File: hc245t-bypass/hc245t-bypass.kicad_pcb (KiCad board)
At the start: 2 copper layers, 6.6 x 4.5 mm, 16 parts

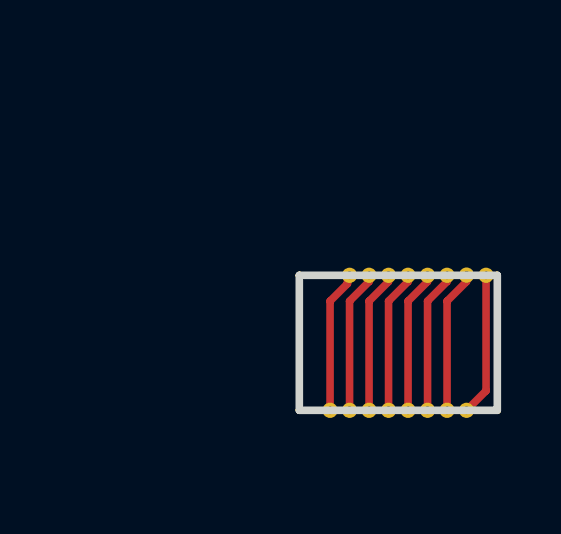
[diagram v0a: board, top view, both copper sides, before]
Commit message: hc245t-bypass: create panel of two to account for oshpark min size
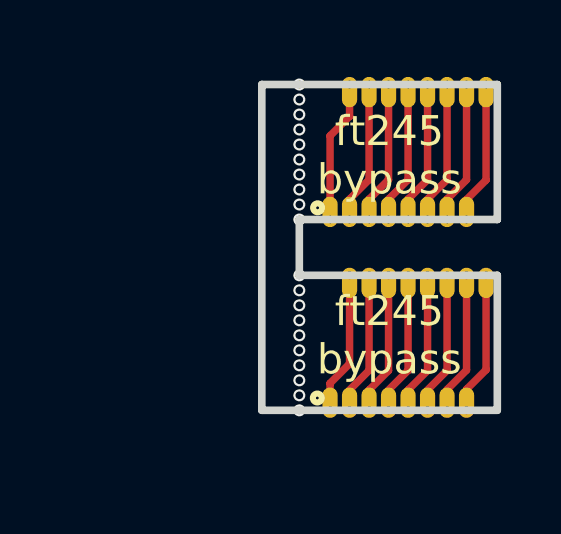
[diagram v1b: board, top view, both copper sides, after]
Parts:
- added TP21: TestPoint, tom-mechanical:Castellation_5.08_2.54, F.Cu at (-2.27, -4.11)
- added TP22: TestPoint, tom-mechanical:Castellation_5.08_2.54, F.Cu at (-1.62, -4.11)
- added TP23: TestPoint, tom-mechanical:Castellation_5.08_2.54, F.Cu at (-0.97, -4.11)
- added TP24: TestPoint, tom-mechanical:Castellation_5.08_2.54, F.Cu at (0.33, -8.61)
- added TP25: TestPoint, tom-mechanical:Castellation_5.08_2.54, F.Cu at (0.33, -4.11)
- added TP26: TestPoint, tom-mechanical:Castellation_5.08_2.54, F.Cu at (0.97, -4.11)
- added TP27: TestPoint, tom-mechanical:Castellation_5.08_2.54, F.Cu at (1.62, -4.11)
- added TP29: TestPoint, tom-mechanical:Castellation_5.08_2.54, F.Cu at (-1.62, -8.61)
- added TP30: TestPoint, tom-mechanical:Castellation_5.08_2.54, F.Cu at (-0.97, -8.61)
- added TP31: TestPoint, tom-mechanical:Castellation_5.08_2.54, F.Cu at (-0.33, -8.61)
- added TP32: TestPoint, tom-mechanical:Castellation_5.08_2.54, F.Cu at (-0.33, -4.11)
- added TP33: TestPoint, tom-mechanical:Castellation_5.08_2.54, F.Cu at (0.97, -8.61)
- added TP34: TestPoint, tom-mechanical:Castellation_5.08_2.54, F.Cu at (1.62, -8.61)
- added TP35: TestPoint, tom-mechanical:Castellation_5.08_2.54, F.Cu at (2.27, -8.61)
- added TP36: TestPoint, tom-mechanical:Castellation_5.08_2.54, F.Cu at (2.92, -8.61)
- added TP9: TestPoint, tom-mechanical:Castellation_5.08_2.54, F.Cu at (2.27, -4.11)
- turned TP2 to 180 degrees
- turned TP3 to 180 degrees
- turned TP4 to 180 degrees
- turned TP5 to 180 degrees
- turned TP6 to 180 degrees
- turned TP7 to 180 degrees
- turned TP8 to 180 degrees
- turned TP9 to 180 degrees
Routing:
- net /a7b7: track 0.00 -> 4.77 mm
- net /a6b6: track 0.00 -> 4.77 mm
- net /a5b5: track 0.00 -> 4.77 mm
- net /a4b4: track 0.00 -> 4.77 mm
- net /a3b3: track 0.00 -> 4.77 mm
- net /a2b2: track 0.00 -> 4.77 mm
- net /a1b1: track 0.00 -> 4.77 mm
- net /a0b0: track 0.00 -> 4.77 mm
- net (no net): vias 0 -> 20
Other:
- board size 6.6 x 4.5 mm -> 7.8 x 10.9 mm
- rule via_min_drill: 0.3 -> 0.254
- board text added: "Jan2020"
- board text added: "ft245 bypass"

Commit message: hc245t-bypass: Feb 2020 version, increase spacing between boards
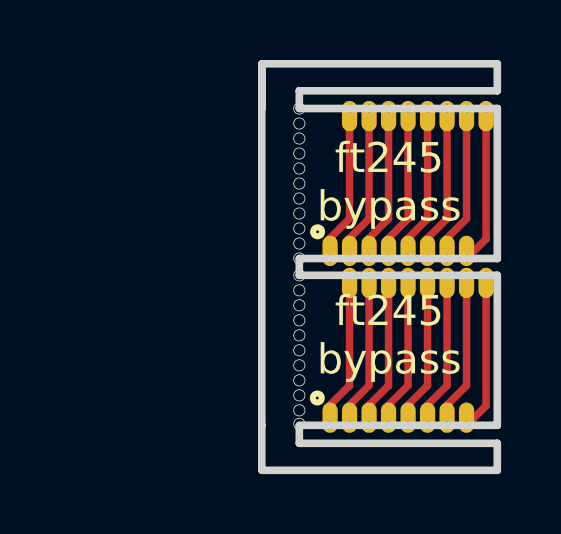
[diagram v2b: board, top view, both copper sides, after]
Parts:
- moved TP21 1.30 mm to (-2.27, -2.81)
- moved TP22 1.30 mm to (-1.62, -2.81)
- moved TP23 1.30 mm to (-0.97, -2.81)
- moved TP25 1.30 mm to (0.33, -2.81)
- moved TP26 1.30 mm to (0.97, -2.81)
- moved TP27 1.30 mm to (1.62, -2.81)
- moved TP32 1.30 mm to (-0.33, -2.81)
- moved TP9 1.30 mm to (2.27, -2.81)
- moved TP24 0.80 mm to (0.33, -7.81)
- moved TP29 0.80 mm to (-1.62, -7.81)
- moved TP30 0.80 mm to (-0.97, -7.81)
- moved TP31 0.80 mm to (-0.33, -7.81)
- moved TP33 0.80 mm to (0.97, -7.81)
- moved TP34 0.80 mm to (1.62, -7.81)
- moved TP35 0.80 mm to (2.27, -7.81)
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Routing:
- net /A2B2: track 4.77 -> 5.28 mm
- net /A0B0: track 4.77 -> 5.28 mm
- net /a7b7: track 4.77 -> 5.27 mm
- net /a6b6: track 4.77 -> 5.27 mm
- net /a5b5: track 4.77 -> 5.27 mm
- net /a4b4: track 4.77 -> 5.27 mm
- net /a3b3: track 4.77 -> 5.27 mm
- net /a2b2: track 4.77 -> 5.27 mm
- net /a1b1: track 4.77 -> 5.27 mm
- net /a0b0: track 4.77 -> 5.27 mm
- net /A7B7: track 4.77 -> 5.27 mm
- net /A5B5: track 4.77 -> 5.27 mm
- net /A4B4: track 4.77 -> 5.27 mm
- net /A3B3: track 4.77 -> 5.27 mm
- net /A1B1: track 4.77 -> 5.27 mm
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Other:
- board size 7.8 x 10.9 mm -> 7.8 x 13.6 mm
- board text added: "Feb2020"
- board text removed: "Jan2020"

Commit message: hc245t-bypass: revert to Jan2018 version for flex pcb
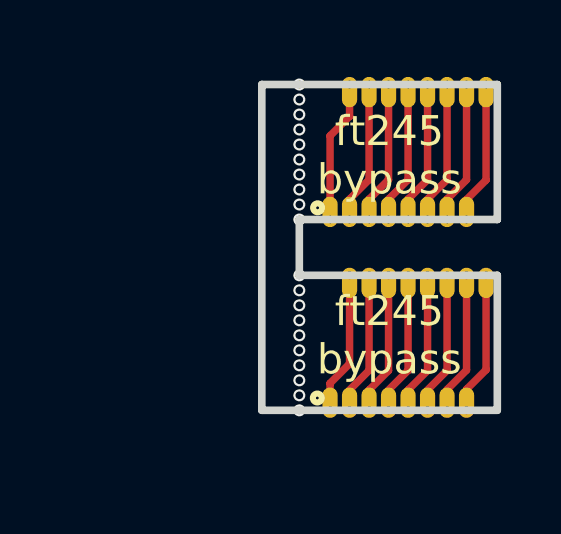
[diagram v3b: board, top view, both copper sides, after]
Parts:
- moved TP21 1.30 mm to (-2.27, -4.11)
- moved TP22 1.30 mm to (-1.62, -4.11)
- moved TP23 1.30 mm to (-0.97, -4.11)
- moved TP25 1.30 mm to (0.33, -4.11)
- moved TP26 1.30 mm to (0.97, -4.11)
- moved TP27 1.30 mm to (1.62, -4.11)
- moved TP32 1.30 mm to (-0.33, -4.11)
- moved TP9 1.30 mm to (2.27, -4.11)
- moved TP24 0.80 mm to (0.33, -8.61)
- moved TP29 0.80 mm to (-1.62, -8.61)
- moved TP30 0.80 mm to (-0.97, -8.61)
- moved TP31 0.80 mm to (-0.33, -8.61)
- moved TP33 0.80 mm to (0.97, -8.61)
- moved TP34 0.80 mm to (1.62, -8.61)
- moved TP35 0.80 mm to (2.27, -8.61)
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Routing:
- net /A2B2: track 5.28 -> 4.77 mm
- net /A0B0: track 5.28 -> 4.77 mm
- net /a7b7: track 5.27 -> 4.77 mm
- net /a6b6: track 5.27 -> 4.77 mm
- net /a5b5: track 5.27 -> 4.77 mm
- net /a4b4: track 5.27 -> 4.77 mm
- net /a3b3: track 5.27 -> 4.77 mm
- net /a2b2: track 5.27 -> 4.77 mm
- net /a1b1: track 5.27 -> 4.77 mm
- net /a0b0: track 5.27 -> 4.77 mm
- net /A7B7: track 5.27 -> 4.77 mm
- net /A5B5: track 5.27 -> 4.77 mm
- net /A4B4: track 5.27 -> 4.77 mm
- net /A3B3: track 5.27 -> 4.77 mm
- net /A1B1: track 5.27 -> 4.77 mm
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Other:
- board size 7.8 x 13.6 mm -> 7.8 x 10.9 mm
- board text added: "Jan2020"
- board text removed: "Feb2020"

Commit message: hc245t-bypass : flex version as submitted to oshpark for Feb 2020
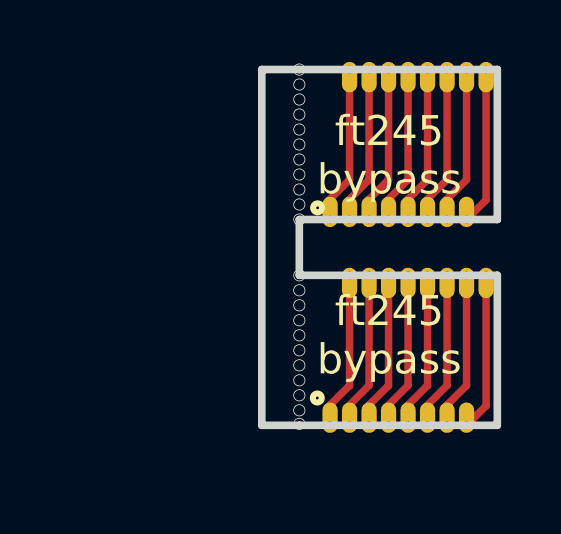
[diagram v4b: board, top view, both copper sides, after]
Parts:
- moved TP2 0.50 mm to (-2.27, 2.75)
- moved TP24 0.50 mm to (0.33, -9.11)
- moved TP29 0.50 mm to (-1.62, -9.11)
- moved TP3 0.50 mm to (-1.62, 2.75)
- moved TP30 0.50 mm to (-0.97, -9.11)
- moved TP31 0.50 mm to (-0.33, -9.11)
- moved TP33 0.50 mm to (0.97, -9.11)
- moved TP34 0.50 mm to (1.62, -9.11)
- moved TP35 0.50 mm to (2.27, -9.11)
- moved TP36 0.50 mm to (2.92, -9.11)
- moved TP4 0.50 mm to (-0.97, 2.75)
- moved TP5 0.50 mm to (-0.33, 2.75)
- moved TP6 0.50 mm to (0.33, 2.75)
- moved TP7 0.50 mm to (0.97, 2.75)
- moved TP8 0.50 mm to (1.62, 2.75)
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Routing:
- net /A2B2: track 4.77 -> 5.28 mm
- net /A0B0: track 4.77 -> 5.28 mm
- net /a7b7: track 4.77 -> 5.27 mm
- net /a6b6: track 4.77 -> 5.27 mm
- net /a5b5: track 4.77 -> 5.27 mm
- net /a4b4: track 4.77 -> 5.27 mm
- net /a3b3: track 4.77 -> 5.27 mm
- net /a2b2: track 4.77 -> 5.27 mm
- net /a1b1: track 4.77 -> 5.27 mm
- net /a0b0: track 4.77 -> 5.27 mm
- net /A7B7: track 4.77 -> 5.27 mm
- net /A5B5: track 4.77 -> 5.27 mm
- net /A4B4: track 4.77 -> 5.27 mm
- net /A3B3: track 4.77 -> 5.27 mm
- net /A1B1: track 4.77 -> 5.27 mm
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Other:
- board size 7.8 x 10.9 mm -> 7.8 x 11.9 mm
- board text added: "Feb2020"
- board text removed: "Jan2020"

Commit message: hc245t-bypass: Mar2020 rev with 4 instances
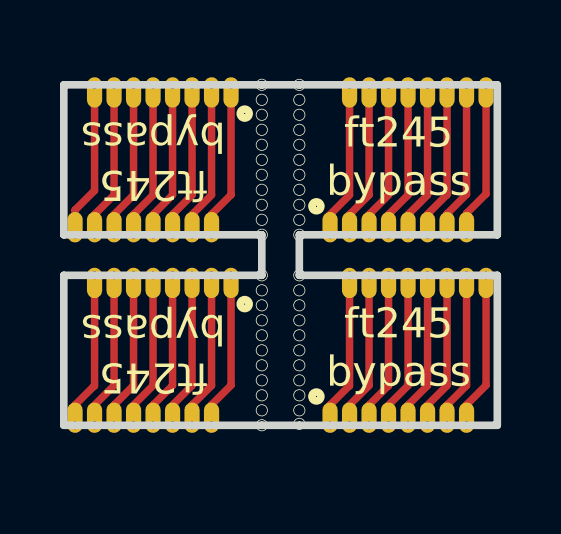
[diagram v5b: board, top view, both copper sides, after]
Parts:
- added TP33: TestPoint, tom-mechanical:Castellation_5.08_2.54, F.Cu at (-5.58, -2.25)
- added TP34: TestPoint, tom-mechanical:Castellation_5.08_2.54, F.Cu at (-6.22, -2.25)
- added TP35: TestPoint, tom-mechanical:Castellation_5.08_2.54, F.Cu at (-6.88, -2.25)
- added TP36: TestPoint, tom-mechanical:Castellation_5.08_2.54, F.Cu at (-7.53, -2.25)
- added TP37: TestPoint, tom-mechanical:Castellation_5.08_2.54, F.Cu at (-8.18, -2.25)
- added TP38: TestPoint, tom-mechanical:Castellation_5.08_2.54, F.Cu at (-8.82, -2.25)
- added TP39: TestPoint, tom-mechanical:Castellation_5.08_2.54, F.Cu at (-9.47, -2.25)
- added TP40: TestPoint, tom-mechanical:Castellation_5.08_2.54, F.Cu at (-10.1, -2.25)
- added TP41: TestPoint, tom-mechanical:Castellation_5.08_2.54, F.Cu at (-6.22, 2.75)
- added TP42: TestPoint, tom-mechanical:Castellation_5.08_2.54, F.Cu at (-6.88, 2.75)
- added TP43: TestPoint, tom-mechanical:Castellation_5.08_2.54, F.Cu at (-7.53, 2.75)
- added TP44: TestPoint, tom-mechanical:Castellation_5.08_2.54, F.Cu at (-8.18, 2.75)
- added TP45: TestPoint, tom-mechanical:Castellation_5.08_2.54, F.Cu at (-8.82, 2.75)
- added TP46: TestPoint, tom-mechanical:Castellation_5.08_2.54, F.Cu at (-9.47, 2.75)
- added TP47: TestPoint, tom-mechanical:Castellation_5.08_2.54, F.Cu at (-10.1, 2.75)
- added TP48: TestPoint, tom-mechanical:Castellation_5.08_2.54, F.Cu at (-10.8, 2.75)
- added TP49: TestPoint, tom-mechanical:Castellation_5.08_2.54, F.Cu at (-5.58, -8.60)
- added TP50: TestPoint, tom-mechanical:Castellation_5.08_2.54, F.Cu at (-6.22, -8.60)
- added TP51: TestPoint, tom-mechanical:Castellation_5.08_2.54, F.Cu at (-6.88, -8.60)
- added TP52: TestPoint, tom-mechanical:Castellation_5.08_2.54, F.Cu at (-7.53, -8.60)
- added TP53: TestPoint, tom-mechanical:Castellation_5.08_2.54, F.Cu at (-8.18, -8.60)
- added TP54: TestPoint, tom-mechanical:Castellation_5.08_2.54, F.Cu at (-8.82, -8.60)
- added TP55: TestPoint, tom-mechanical:Castellation_5.08_2.54, F.Cu at (-9.47, -8.60)
- added TP56: TestPoint, tom-mechanical:Castellation_5.08_2.54, F.Cu at (-10.1, -8.60)
- added TP57: TestPoint, tom-mechanical:Castellation_5.08_2.54, F.Cu at (-6.22, -3.60)
- added TP58: TestPoint, tom-mechanical:Castellation_5.08_2.54, F.Cu at (-6.88, -3.60)
- added TP59: TestPoint, tom-mechanical:Castellation_5.08_2.54, F.Cu at (-7.53, -3.60)
- added TP60: TestPoint, tom-mechanical:Castellation_5.08_2.54, F.Cu at (-8.18, -3.60)
- added TP61: TestPoint, tom-mechanical:Castellation_5.08_2.54, F.Cu at (-8.82, -3.60)
- added TP62: TestPoint, tom-mechanical:Castellation_5.08_2.54, F.Cu at (-9.47, -3.60)
- added TP63: TestPoint, tom-mechanical:Castellation_5.08_2.54, F.Cu at (-10.1, -3.60)
- added TP64: TestPoint, tom-mechanical:Castellation_5.08_2.54, F.Cu at (-10.8, -3.60)
- moved TP17 0.51 mm to (-2.27, -3.60)
- moved TP18 0.51 mm to (-1.62, -3.60)
- moved TP19 0.51 mm to (-0.97, -3.60)
- moved TP21 0.51 mm to (0.33, -3.60)
- moved TP22 0.51 mm to (0.97, -3.60)
- moved TP23 0.51 mm to (1.62, -3.60)
- moved TP24 0.51 mm to (2.27, -3.60)
- moved TP28 0.51 mm to (-0.33, -3.60)
- moved TP20 0.51 mm to (0.33, -8.60)
- moved TP25 0.51 mm to (-1.62, -8.60)
- moved TP26 0.51 mm to (-0.97, -8.60)
- moved TP27 0.51 mm to (-0.33, -8.60)
- moved TP29 0.51 mm to (0.97, -8.60)
- moved TP30 0.51 mm to (1.62, -8.60)
- moved TP31 0.51 mm to (2.27, -8.60)
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- renumbered TP2 to TP1, TP17 to TP10, TP16 to TP11, TP15 to TP12, TP14 to TP13, TP13 to TP14, TP12 to TP15, TP11 to TP16, TP21 to TP17, TP22 to TP18, TP23 to TP19, TP3 to TP2, TP24 to TP20, TP25 to TP21, TP26 to TP22, TP27 to TP23, TP9 to TP24, TP29 to TP25, TP30 to TP26, TP31 to TP27, TP32 to TP28, TP33 to TP29, TP4 to TP3, TP34 to TP30, TP35 to TP31, TP36 to TP32, TP5 to TP4, TP6 to TP5, TP7 to TP6, TP8 to TP7, TP9 to TP8, TP18 to TP9
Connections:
- net /A0B0 renamed /A0B0_1
- net /A1B1 renamed /A1B1_1
- net /A2B2 renamed /A2B2_1
- net /A3B3 renamed /A3B3_1
- net /A4B4 renamed /A4B4_1
- net /A5B5 renamed /A5B5_1
- net /A6B6 renamed /A6B6_1
- net /A7B7 renamed /A7B7_1
- net /a0b0 renamed /A1B1_2
- net /a1b1 renamed /A2B2_2
- net /a2b2 renamed /A3B3_2
- net /a3b3 renamed /A4B4_2
- net /a4b4 renamed /A5B5_2
- net /a5b5 renamed /A6B6_2
- net /a6b6 renamed /A7B7_2
- net /a7b7 renamed /A8B8_2
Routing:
- net /A8B8_3: track 0.00 -> 5.28 mm
- net /A8B8_4: track 0.00 -> 5.27 mm
- net /A7B7_4: track 0.00 -> 5.27 mm
- net /A7B7_3: track 0.00 -> 5.27 mm
- net /A6B6_4: track 0.00 -> 5.27 mm
- net /A6B6_3: track 0.00 -> 5.27 mm
- net /A4B4_4: track 0.00 -> 5.27 mm
- net /A4B4_3: track 0.00 -> 5.27 mm
- net /A3B3_4: track 0.00 -> 5.27 mm
- net /A3B3_3: track 0.00 -> 5.27 mm
- net /A2B2_4: track 0.00 -> 5.27 mm
- net /A2B2_3: track 0.00 -> 5.27 mm
- net /A1B1_3: track 0.00 -> 5.27 mm
- net /A5B5_4: track 0.00 -> 5.27 mm
- net /A5B5_3: track 0.00 -> 5.27 mm
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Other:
- board size 7.8 x 11.9 mm -> 14.4 x 11.3 mm
- board text added: "Mar2020"
- board text removed: "Feb2020"

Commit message: hc245t-bypass.kicad_pcb: fix solder mask settings
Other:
- rule pad_to_mask_clearance: 0.051 -> 0.0508
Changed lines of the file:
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@@
     (pad_size 0.508 0.508)
     (pad_drill 0.254)
-    (pad_to_mask_clearance 0.051)
-    (solder_mask_min_width 0.25)
+    (pad_to_mask_clearance 0.0508)
     (aux_axis_origin 93.3 105)
     (grid_origin -3.3 -2.25)
